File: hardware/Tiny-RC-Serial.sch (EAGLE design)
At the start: 12 parts, among them IC1 ATTINY84A-SSU

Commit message: updated readme and sch and brd
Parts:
- renumbered C3 to C1
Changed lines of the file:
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@@
 <?xml version="1.0" encoding="utf-8"?>
 <!DOCTYPE eagle SYSTEM "eagle.dtd">
-<eagle version="6.2">
+<eagle version="6.3">
 <drawing>
 <settings>
@@
 <part name="GND3" library="SparkFun" deviceset="GND" device=""/>
 <part name="U$3" library="SparkFun" deviceset="5V" device=""/>
-<part name="C3" library="SparkFun" deviceset="CAP" device="PTH" value="0.1uF"/>
+<part name="C1" library="SparkFun" deviceset="CAP" device="PTH" value="0.1uF"/>
 <part name="JP2" library="pinhead" deviceset="PINHD-2X3" device=""/>
 <part name="GND5" library="SparkFun" deviceset="GND" device=""/>
@@
 <instance part="GND3" gate="1" x="68.58" y="78.74"/>
 <instance part="U$3" gate="G$1" x="55.88" y="119.38"/>
-<instance part="C3" gate="G$1" x="55.88" y="93.98"/>
+<instance part="C1" gate="G$1" x="55.88" y="93.98"/>
 <instance part="JP2" gate="A" x="88.9" y="134.62" rot="MR0"/>
 <instance part="GND5" gate="1" x="71.12" y="121.92"/>
@@
 <wire x1="73.66" y1="101.6" x2="55.88" y2="101.6" width="0.1524" layer="91"/>
 <wire x1="55.88" y1="101.6" x2="55.88" y2="119.38" width="0.1524" layer="91"/>
-<pinref part="C3" gate="G$1" pin="1"/>
+<pinref part="C1" gate="G$1" pin="1"/>
 <wire x1="55.88" y1="101.6" x2="55.88" y2="99.06" width="0.1524" layer="91"/>
 <junction x="55.88" y="101.6"/>
@@
 <segment>
 <pinref part="GND3" gate="1" pin="GND"/>
-<pinref part="C3" gate="G$1" pin="2"/>
+<pinref part="C1" gate="G$1" pin="2"/>
 <wire x1="68.58" y1="88.9" x2="68.58" y2="81.28" width="0.1524" layer="91"/>
 <wire x1="55.88" y1="91.44" x2="55.88" y2="88.9" width="0.1524" layer="91"/>

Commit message: updated to version 3.0
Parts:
- added C2, C3: .22uF, SparkFun-Capacitors:CAP0805
- added Y1: 20Mhz, SparkFun-FreqCtrl:CRYSTALHC49US
- JP3: device jst-ph:JST-PH4 -> SparkFun-Connectors:M03PTH
- R1: device rcl:R-US_R1206 -> SparkFun-Resistors:RESISTOR0805-RES
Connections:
- removed net RST: IC1.(RESET/DW)PB3, JP2.5
- removed net RX: IC1.(XTAL2)PB1, JP3.2
- new net N$3: C2.1, IC1.(XTAL1/CLKI)PB0, Y1.2
- new net N$4: C3.1, IC1.(XTAL2)PB1, Y1.1
- new net RCDATA: IC1.(RESET/DW)PB3, JP1.5, JP2.5
- net GND: now also C2.2, C3.2, JP3.1; no longer JP3.4
- net TX: now also IC1.(INT0/OC0A/CKOUT)PB2, JP3.2; no longer IC1.(XTAL1/CLKI)PB0, JP3.3
- net VIN: now also JP3.3; no longer JP3.1
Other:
- moved on the sheet: LED1, R1
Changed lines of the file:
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@@
 <setting verticaltext="up"/>
 </settings>
-<grid distance="0.1" unitdist="inch" unit="inch" style="dots" multiple="1" display="yes" altdistance="0.01" altunitdist="inch" altunit="inch"/>
+<grid distance="0.1" unitdist="inch" unit="inch" style="lines" multiple="1" display="no" altdistance="0.01" altunitdist="inch" altunit="inch"/>
 <layers>
 <layer number="1" name="Top" color="4" fill="1" visible="no" active="no"/>
@@
 <layer number="144" name="Drill_legend" color="7" fill="1" visible="no" active="yes"/>
 <layer number="151" name="HeatSink" color="7" fill="1" visible="no" active="yes"/>
+<layer number="199" name="Contour" color="7" fill="1" visible="yes" active="yes"/>
 <layer number="200" name="200bmp" color="1" fill="10" visible="no" active="yes"/>
 <layer number="201" name="201bmp" color="2" fill="10" visible="no" active="yes"/>
@@
 <part name="GND5" library="SparkFun" deviceset="GND" device=""/>
 <part name="IC1" library="attiny" deviceset="ATTINY84A-SSU" device=""/>
-<part name="JP3" library="jst-ph" deviceset="JST-PH4" device=""/>
 <part name="GND1" library="SparkFun" deviceset="GND" device=""/>
 <part name="LED1" library="led" deviceset="LED" device="SML1206"/>
-<part name="R1" library="rcl" deviceset="R-US_" device="R1206" value="330"/>
+<part name="R1" library="SparkFun-Resistors" deviceset="RESISTOR" device="0805-RES" value="330"/>
 <part name="GND6" library="SparkFun" deviceset="GND" device=""/>
 <part name="D1" library="SparkFun" deviceset="DIODE" device="SOD"/>
 <part name="U$4" library="SparkFun" deviceset="5V" device=""/>
+<part name="Y1" library="SparkFun-FreqCtrl" deviceset="CRYSTAL" device="HC49US" value="20Mhz"/>
+<part name="C2" library="SparkFun-Capacitors" deviceset="CAP" device="0805" value=".22uF"/>
+<part name="C3" library="SparkFun-Capacitors" deviceset="CAP" device="0805" value=".22uF"/>
+<part name="GND4" library="SparkFun" deviceset="GND" device=""/>
+<part name="JP3" library="SparkFun-Connectors" deviceset="M03" device="PTH"/>
 </parts>
 <sheets>
@@
 <instances>
 <instance part="JP1" gate="A" x="33.02" y="60.96"/>
-<instance part="U$1" gate="G$1" x="172.72" y="137.16"/>
+<instance part="U$1" gate="G$1" x="210.82" y="139.7"/>
 <instance part="U$2" gate="G$1" x="12.7" y="73.66"/>
 <instance part="GND2" gate="1" x="48.26" y="38.1"/>
@@
 <instance part="GND5" gate="1" x="71.12" y="121.92"/>
 <instance part="IC1" gate="G$1" x="93.98" y="73.66"/>
-<instance part="JP3" gate="A" x="20.32" y="134.62"/>
 <instance part="GND1" gate="1" x="35.56" y="121.92"/>
-<instance part="LED1" gate="G$1" x="172.72" y="104.14"/>
-<instance part="R1" gate="G$1" x="172.72" y="116.84" rot="R90"/>
-<instance part="GND6" gate="1" x="172.72" y="88.9"/>
+<instance part="LED1" gate="G$1" x="210.82" y="106.68"/>
+<instance part="R1" gate="G$1" x="210.82" y="119.38" rot="R90"/>
+<instance part="GND6" gate="1" x="210.82" y="91.44"/>
 <instance part="D1" gate="G$1" x="53.34" y="137.16"/>
 <instance part="U$4" gate="G$1" x="71.12" y="147.32"/>
+<instance part="Y1" gate="G$1" x="162.56" y="99.06" smashed="yes" rot="R90">
+<attribute name="NAME" x="160.02" y="103.124" size="1.778" layer="95" rot="R180"/>
+<attribute name="VALUE" x="160.02" y="99.06" size="1.778" layer="96" rot="R180"/>
+</instance>
+<instance part="C2" gate="G$1" x="172.72" y="104.14" smashed="yes" rot="R90">
+<attribute name="NAME" x="168.656" y="106.299" size="1.778" layer="95" rot="R180"/>
+<attribute name="VALUE" x="181.356" y="106.299" size="1.778" layer="96" rot="R180"/>
+</instance>
+<instance part="C3" gate="G$1" x="172.72" y="93.98" smashed="yes" rot="R90">
+<attribute name="NAME" x="168.656" y="96.139" size="1.778" layer="95" rot="R180"/>
+<attribute name="VALUE" x="181.356" y="96.139" size="1.778" layer="96" rot="R180"/>
+</instance>
+<instance part="GND4" gate="1" x="182.88" y="86.36"/>
+<instance part="JP3" gate="G$1" x="17.78" y="134.62"/>
 </instances>
 <busses>
@@
 <pinref part="U$1" gate="G$1" pin="5V"/>
 <pinref part="R1" gate="G$1" pin="2"/>
-<wire x1="172.72" y1="137.16" x2="172.72" y2="121.92" width="0.1524" layer="91"/>
+<wire x1="210.82" y1="139.7" x2="210.82" y2="124.46" width="0.1524" layer="91"/>
 </segment>
 <segment>
@@
 </segment>
 <segment>
-<pinref part="JP3" gate="A" pin="4"/>
-<wire x1="27.94" y1="129.54" x2="35.56" y2="129.54" width="0.1524" layer="91"/>
-<wire x1="35.56" y1="129.54" x2="35.56" y2="124.46" width="0.1524" layer="91"/>
+<wire x1="25.4" y1="132.08" x2="35.56" y2="132.08" width="0.1524" layer="91"/>
+<wire x1="35.56" y1="132.08" x2="35.56" y2="124.46" width="0.1524" layer="91"/>
 <pinref part="GND1" gate="1" pin="GND"/>
+<pinref part="JP3" gate="G$1" pin="1"/>
 </segment>
 <segment>
 <pinref part="LED1" gate="G$1" pin="C"/>
 <pinref part="GND6" gate="1" pin="GND"/>
-<wire x1="172.72" y1="99.06" x2="172.72" y2="91.44" width="0.1524" layer="91"/>
+<wire x1="210.82" y1="101.6" x2="210.82" y2="93.98" width="0.1524" layer="91"/>
+</segment>
+<segment>
+<pinref part="C2" gate="G$1" pin="2"/>
+<wire x1="175.26" y1="104.14" x2="182.88" y2="104.14" width="0.1524" layer="91"/>
+<wire x1="182.88" y1="104.14" x2="182.88" y2="93.98" width="0.1524" layer="91"/>
+<pinref part="C3" gate="G$1" pin="2"/>
+<wire x1="182.88" y1="93.98" x2="182.88" y2="88.9" width="0.1524" layer="91"/>
+<wire x1="175.26" y1="93.98" x2="182.88" y2="93.98" width="0.1524" layer="91"/>
+<junction x="182.88" y="93.98"/>
+<pinref part="GND4" gate="1" pin="GND"/>
 </segment>
 </net>
@@
 </segment>
 </net>
-<net name="RX" class="0">
-<segment>
-<pinref part="IC1" gate="G$1" pin="(XTAL2)PB1"/>
-<wire x1="121.92" y1="96.52" x2="139.7" y2="96.52" width="0.1524" layer="91"/>
-<label x="139.7" y="96.52" size="1.778" layer="95" xref="yes"/>
-</segment>
-<segment>
-<pinref part="JP3" gate="A" pin="2"/>
-<wire x1="27.94" y1="134.62" x2="40.64" y2="134.62" width="0.1524" layer="91"/>
-<label x="40.64" y="134.62" size="1.016" layer="95" xref="yes"/>
-</segment>
-</net>
 <net name="TX" class="0">
 <segment>
-<pinref part="IC1" gate="G$1" pin="(XTAL1/CLKI)PB0"/>
-<wire x1="121.92" y1="101.6" x2="139.7" y2="101.6" width="0.1524" layer="91"/>
-<label x="139.7" y="101.6" size="1.778" layer="95" xref="yes"/>
-</segment>
-<segment>
-<pinref part="JP3" gate="A" pin="3"/>
-<wire x1="27.94" y1="132.08" x2="40.64" y2="132.08" width="0.1524" layer="91"/>
-<label x="40.64" y="132.08" size="1.016" layer="95" xref="yes"/>
-</segment>
-</net>
-<net name="RST" class="0">
-<segment>
-<pinref part="JP2" gate="A" pin="5"/>
-<wire x1="91.44" y1="132.08" x2="106.68" y2="132.08" width="0.1524" layer="91"/>
-<label x="106.68" y="132.08" size="1.016" layer="95" xref="yes"/>
-</segment>
-<segment>
-<pinref part="IC1" gate="G$1" pin="(RESET/DW)PB3"/>
-<wire x1="121.92" y1="91.44" x2="139.7" y2="91.44" width="0.1524" layer="91"/>
-<label x="139.7" y="91.44" size="1.778" layer="95" xref="yes"/>
+<wire x1="25.4" y1="134.62" x2="38.1" y2="134.62" width="0.1524" layer="91"/>
+<label x="38.1" y="134.62" size="1.016" layer="95" xref="yes"/>
+<pinref part="JP3" gate="G$1" pin="2"/>
+</segment>
+<segment>
+<pinref part="IC1" gate="G$1" pin="(INT0/OC0A/CKOUT)PB2"/>
+<wire x1="121.92" y1="86.36" x2="139.7" y2="86.36" width="0.1524" layer="91"/>
+<label x="139.7" y="86.36" size="1.778" layer="95" xref="yes"/>
 </segment>
 </net>
@@
 <net name="VIN" class="0">
 <segment>
-<pinref part="JP3" gate="A" pin="1"/>
 <pinref part="D1" gate="G$1" pin="A"/>
-<wire x1="27.94" y1="137.16" x2="50.8" y2="137.16" width="0.1524" layer="91"/>
+<wire x1="25.4" y1="137.16" x2="50.8" y2="137.16" width="0.1524" layer="91"/>
+<pinref part="JP3" gate="G$1" pin="3"/>
 </segment>
 </net>
@@
 <pinref part="R1" gate="G$1" pin="1"/>
 <pinref part="LED1" gate="G$1" pin="A"/>
-<wire x1="172.72" y1="111.76" x2="172.72" y2="106.68" width="0.1524" layer="91"/>
-</segment>
-</net>
+<wire x1="210.82" y1="114.3" x2="210.82" y2="109.22" width="0.1524" layer="91"/>
+</segment>
+</net>
+<net name="RCDATA" class="0">
+<segment>
+<pinref part="JP1" gate="A" pin="5"/>
+<wire x1="30.48" y1="60.96" x2="17.78" y2="60.96" width="0.1524" layer="91"/>
+<label x="17.78" y="60.96" size="1.016" layer="95" rot="R180" xref="yes"/>
+</segment>
+<segment>
+<pinref part="IC1" gate="G$1" pin="(RESET/DW)PB3"/>
+<wire x1="121.92" y1="91.44" x2="127" y2="91.44" width="0.1524" layer="91"/>
+<wire x1="127" y1="91.44" x2="127" y2="132.08" width="0.1524" layer="91"/>
+<pinref part="JP2" gate="A" pin="5"/>
+<wire x1="127" y1="132.08" x2="91.44" y2="132.08" width="0.1524" layer="91"/>
+<wire x1="127" y1="91.44" x2="139.7" y2="91.44" width="0.1524" layer="91"/>
+<junction x="127" y="91.44"/>
+<label x="139.7" y="91.44" size="1.778" layer="95" xref="yes"/>
+</segment>
+</net>
+<net name="N$3" class="0">
+<segment>
+<pinref part="IC1" gate="G$1" pin="(XTAL1/CLKI)PB0"/>
+<wire x1="121.92" y1="101.6" x2="137.16" y2="101.6" width="0.1524" layer="91"/>
+<wire x1="137.16" y1="101.6" x2="137.16" y2="104.14" width="0.1524" layer="91"/>
+<pinref part="C2" gate="G$1" pin="1"/>
+<wire x1="137.16" y1="104.14" x2="162.56" y2="104.14" width="0.1524" layer="91"/>
+<pinref part="Y1" gate="G$1" pin="2"/>
+<wire x1="162.56" y1="104.14" x2="167.64" y2="104.14" width="0.1524" layer="91"/>
+<wire x1="162.56" y1="101.6" x2="162.56" y2="104.14" width="0.1524" layer="91"/>
+<junction x="162.56" y="104.14"/>
+</segment>
+</net>
+<net name="N$4" class="0">
+<segment>
+<pinref part="IC1" gate="G$1" pin="(XTAL2)PB1"/>
+<wire x1="121.92" y1="96.52" x2="137.16" y2="96.52" width="0.1524" layer="91"/>
+<wire x1="137.16" y1="96.52" x2="137.16" y2="93.98" width="0.1524" layer="91"/>
+<pinref part="C3" gate="G$1" pin="1"/>
+<wire x1="137.16" y1="93.98" x2="162.56" y2="93.98" width="0.1524" layer="91"/>
+<pinref part="Y1" gate="G$1" pin="1"/>
+<wire x1="162.56" y1="93.98" x2="167.64" y2="93.98" width="0.1524" layer="91"/>
+<wire x1="162.56" y1="96.52" x2="162.56" y2="93.98" width="0.1524" layer="91"/>
+<junction x="162.56" y="93.98"/>
+</segment>
+</net>

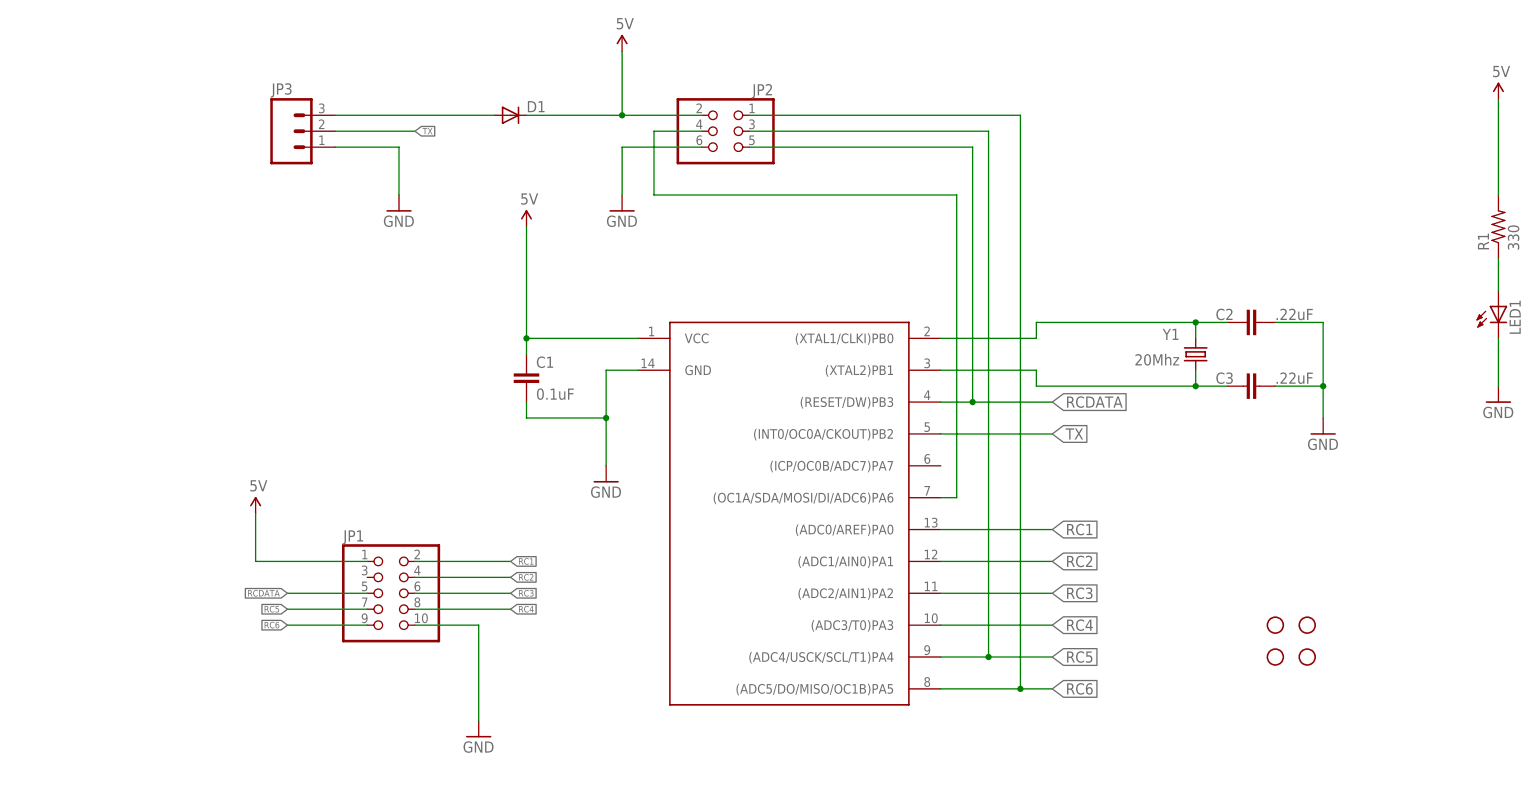
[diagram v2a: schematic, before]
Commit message: updated board to rev 3.0 - now using ATTiny2313
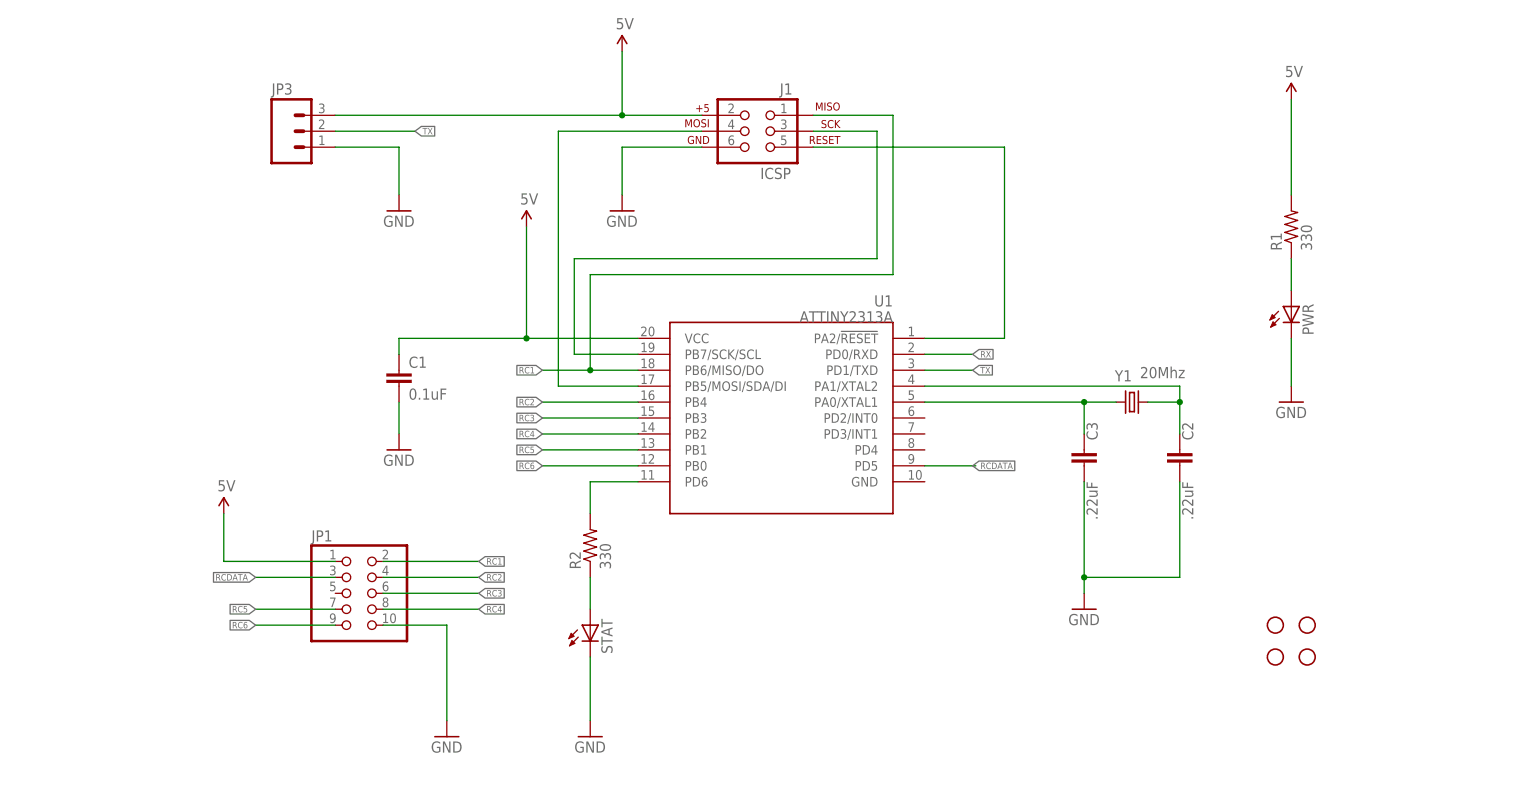
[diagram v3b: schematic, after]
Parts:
- removed D1: (no value), SparkFun:DIODESOD
- removed IC1: ATTINY84A-SSU, attiny:ATTINY84A-SSU
- removed JP2: (no value), pinhead:PINHD-2X3
- removed LED1: (no value), led:LEDSML1206
- added J1: ICSP, SparkFun-Connectors:AVR_SPI_PRG_6PTH
- added PWR, STAT: (no value), SparkFun-LED:LED1206
- added R2: 330, SparkFun-Resistors:RESISTOR1206
- added U1: ATTINY2313A, SparkFun-DigitalIC:ATTINY2313A
- C2, C3: device SparkFun-Capacitors:CAP0805 -> SparkFun-Capacitors:CAP1206
- R1: device SparkFun-Resistors:RESISTOR0805-RES -> SparkFun-Resistors:RESISTOR1206
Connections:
- removed net VIN: D1.A, JP3.3
- new net MOSI: J1.4, U1.PB5/MOSI/SDA/DI
- new net N$5: R2.1, STAT.A
- new net RESET: J1.5, U1.PA2/!RESET
- new net RX: U1.PD0/RXD
- new net SCK: J1.3, U1.PB7/SCK/SCL
- net 5V: now also J1.2, JP3.3, U1.VCC; no longer D1.C, IC1.VCC, JP2.2
- net GND: now also J1.6, PWR.C, STAT.C; no longer IC1.GND, JP2.6, LED1.C
- net N$1: now also R2.2, U1.PD6; no longer IC1.(OC1A/SDA/MOSI/DI/ADC6)PA6, JP2.4
- net N$2: now also PWR.A; no longer LED1.A
- net N$3: now also U1.PA1/XTAL2; no longer IC1.(XTAL1/CLKI)PB0
- net N$4: now also U1.PA0/XTAL1; no longer IC1.(XTAL2)PB1
- net RC1: now also J1.1, U1.PB6/MISO/DO; no longer IC1.(ADC0/AREF)PA0
- net RC2: now also U1.PB4; no longer IC1.(ADC1/AIN0)PA1
- net RC3: now also U1.PB3; no longer IC1.(ADC2/AIN1)PA2
- net RC4: now also U1.PB2; no longer IC1.(ADC3/T0)PA3
- net RC5: now also U1.PB1; no longer IC1.(ADC4/USCK/SCL/T1)PA4, JP2.3
- net RC6: now also U1.PB0; no longer IC1.(ADC5/DO/MISO/OC1B)PA5, JP2.1
- net RCDATA: now also JP1.3, U1.PD5; no longer IC1.(RESET/DW)PB3, JP1.5, JP2.5
- net TX: now also U1.PD1/TXD; no longer IC1.(INT0/OC0A/CKOUT)PB2
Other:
- moved on the sheet: C1, C2, C3, JP1, R1, Y1
